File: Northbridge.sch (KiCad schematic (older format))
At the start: 25 parts, among them J3 JTAG

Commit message: Squiggles! Silk!
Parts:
- renumbered C106 to C301, C98 to C302, C99 to C303, C107 to C304, C100 to C305, C101 to C306, C115 to C307, C108 to C308, C102 to C309, C103 to C310, C109 to C311, C104 to C312, C105 to C313, C182 to C314, C184 to C315, C185 to C316, J3 to J301, R110 to R301, R111 to R302, R107 to R303, R39 to R304, R40 to R305, R118 to R306
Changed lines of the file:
@@
 AR Path="/5765B2E6/5799D8BC" Ref="C?"  Part="1"
 AR Path="/5763AB3B/5799D8BC" Ref="C?"  Part="1"
-AR Path="/5763A638/5799D8BC" Ref="C98"  Part="1"
-F 0 "C98" H 4513 13946 50  0000 L CNN
+AR Path="/5763A638/5799D8BC" Ref="C302"  Part="1"
+F 0 "C302" H 4513 13946 50  0000 L CNN
 F 1 "1u" H 4513 13855 50  0000 L CNN
 F 2 "IPC7351-Nominal:CAPC1005X55" H 4400 13900 50  0001 C CNN
@@
 AR Path="/5765B2E6/5799D8C4" Ref="C?"  Part="1"
 AR Path="/5763AB3B/5799D8C4" Ref="C?"  Part="1"
-AR Path="/5763A638/5799D8C4" Ref="C100"  Part="1"
-F 0 "C100" H 4913 13946 50  0000 L CNN
+AR Path="/5763A638/5799D8C4" Ref="C305"  Part="1"
+F 0 "C305" H 4913 13946 50  0000 L CNN
 F 1 "1u" H 4913 13855 50  0000 L CNN
 F 2 "IPC7351-Nominal:CAPC1005X55" H 4800 13900 50  0001 C CNN
@@
 AR Path="/5765B2E6/5799D8CC" Ref="C?"  Part="1"
 AR Path="/5763AB3B/5799D8CC" Ref="C?"  Part="1"
-AR Path="/5763A638/5799D8CC" Ref="C102"  Part="1"
-F 0 "C102" H 5313 13946 50  0000 L CNN
+AR Path="/5763A638/5799D8CC" Ref="C309"  Part="1"
+F 0 "C309" H 5313 13946 50  0000 L CNN
 F 1 "1u" H 5313 13855 50  0000 L CNN
 F 2 "IPC7351-Nominal:CAPC1005X55" H 5200 13900 50  0001 C CNN
@@
 AR Path="/5765B2E6/5799D8D4" Ref="C?"  Part="1"
 AR Path="/5763AB3B/5799D8D4" Ref="C?"  Part="1"
-AR Path="/5763A638/5799D8D4" Ref="C104"  Part="1"
-F 0 "C104" H 5713 13946 50  0000 L CNN
+AR Path="/5763A638/5799D8D4" Ref="C312"  Part="1"
+F 0 "C312" H 5713 13946 50  0000 L CNN
 F 1 "1u" H 5713 13855 50  0000 L CNN
 F 2 "IPC7351-Nominal:CAPC1005X55" H 5600 13900 50  0001 C CNN
@@
 AR Path="/5765B2E6/5799D8DC" Ref="C?"  Part="1"
 AR Path="/5763AB3B/5799D8DC" Ref="C?"  Part="1"
-AR Path="/5763A638/5799D8DC" Ref="C99"  Part="1"
-F 0 "C99" H 4513 14446 50  0000 L CNN
+AR Path="/5763A638/5799D8DC" Ref="C303"  Part="1"
+F 0 "C303" H 4513 14446 50  0000 L CNN
 F 1 "1u" H 4513 14355 50  0000 L CNN
 F 2 "IPC7351-Nominal:CAPC1005X55" H 4400 14400 50  0001 C CNN
@@
 AR Path="/5765B2E6/5799D8E4" Ref="C?"  Part="1"
 AR Path="/5763AB3B/5799D8E4" Ref="C?"  Part="1"
-AR Path="/5763A638/5799D8E4" Ref="C101"  Part="1"
-F 0 "C101" H 4913 14446 50  0000 L CNN
+AR Path="/5763A638/5799D8E4" Ref="C306"  Part="1"
+F 0 "C306" H 4913 14446 50  0000 L CNN
 F 1 "1u" H 4913 14355 50  0000 L CNN
 F 2 "IPC7351-Nominal:CAPC1005X55" H 4800 14400 50  0001 C CNN
@@
 AR Path="/5765B2E6/5799D8EC" Ref="C?"  Part="1"
 AR Path="/5763AB3B/5799D8EC" Ref="C?"  Part="1"
-AR Path="/5763A638/5799D8EC" Ref="C103"  Part="1"
-F 0 "C103" H 5313 14446 50  0000 L CNN
+AR Path="/5763A638/5799D8EC" Ref="C310"  Part="1"
+F 0 "C310" H 5313 14446 50  0000 L CNN
 F 1 "1u" H 5313 14355 50  0000 L CNN
 F 2 "IPC7351-Nominal:CAPC1005X55" H 5200 14400 50  0001 C CNN
@@
 AR Path="/5765B2E6/5799D8F4" Ref="C?"  Part="1"
 AR Path="/5763AB3B/5799D8F4" Ref="C?"  Part="1"
-AR Path="/5763A638/5799D8F4" Ref="C105"  Part="1"
-F 0 "C105" H 5713 14446 50  0000 L CNN
+AR Path="/5763A638/5799D8F4" Ref="C313"  Part="1"
+F 0 "C313" H 5713 14446 50  0000 L CNN
 F 1 "1u" H 5713 14355 50  0000 L CNN
 F 2 "IPC7351-Nominal:CAPC1005X55" H 5600 14400 50  0001 C CNN
@@
 P 5900 14700
 AR Path="/5763AB3B/5799D8FC" Ref="#PWR?"  Part="1"
-AR Path="/5763A638/5799D8FC" Ref="#PWR273"  Part="1"
-F 0 "#PWR273" H 5900 14700 30  0001 C CNN
+AR Path="/5763A638/5799D8FC" Ref="#PWR302"  Part="1"
+F 0 "#PWR302" H 5900 14700 30  0001 C CNN
 F 1 "GND" H 5900 14630 30  0001 C CNN
 F 2 "" H 5900 14700 60  0000 C CNN
@@
 AR Path="/5765B2E6/5799E7E9" Ref="C?"  Part="1"
 AR Path="/5763AB3B/5799E7E9" Ref="C?"  Part="1"
-AR Path="/5763A638/5799E7E9" Ref="C106"  Part="1"
-F 0 "C106" H 4513 12596 50  0000 L CNN
+AR Path="/5763A638/5799E7E9" Ref="C301"  Part="1"
+F 0 "C301" H 4513 12596 50  0000 L CNN
 F 1 "1u" H 4513 12505 50  0000 L CNN
 F 2 "IPC7351-Nominal:CAPC1005X55" H 4400 12550 50  0001 C CNN
@@
 AR Path="/5765B2E6/5799E7F0" Ref="C?"  Part="1"
 AR Path="/5763AB3B/5799E7F0" Ref="C?"  Part="1"
-AR Path="/5763A638/5799E7F0" Ref="C107"  Part="1"
-F 0 "C107" H 4913 12596 50  0000 L CNN
+AR Path="/5763A638/5799E7F0" Ref="C304"  Part="1"
+F 0 "C304" H 4913 12596 50  0000 L CNN
 F 1 "1u" H 4913 12505 50  0000 L CNN
 F 2 "IPC7351-Nominal:CAPC1005X55" H 4800 12550 50  0001 C CNN
@@
 AR Path="/5765B2E6/5799E7F7" Ref="C?"  Part="1"
 AR Path="/5763AB3B/5799E7F7" Ref="C?"  Part="1"
-AR Path="/5763A638/5799E7F7" Ref="C108"  Part="1"
-F 0 "C108" H 5313 12596 50  0000 L CNN
+AR Path="/5763A638/5799E7F7" Ref="C308"  Part="1"
+F 0 "C308" H 5313 12596 50  0000 L CNN
 F 1 "1u" H 5313 12505 50  0000 L CNN
 F 2 "IPC7351-Nominal:CAPC1005X55" H 5200 12550 50  0001 C CNN
@@
 AR Path="/5765B2E6/5799E7FE" Ref="C?"  Part="1"
 AR Path="/5763AB3B/5799E7FE" Ref="C?"  Part="1"
-AR Path="/5763A638/5799E7FE" Ref="C109"  Part="1"
-F 0 "C109" H 5713 12596 50  0000 L CNN
+AR Path="/5763A638/5799E7FE" Ref="C311"  Part="1"
+F 0 "C311" H 5713 12596 50  0000 L CNN
 F 1 "1u" H 5713 12505 50  0000 L CNN
 F 2 "IPC7351-Nominal:CAPC1005X55" H 5600 12550 50  0001 C CNN
@@
 P3V3_BRIDGE
 $Comp
-L GND #PWR272
+L GND #PWR301
 U 1 1 5799E8A3
 P 5600 12850
-F 0 "#PWR272" H 5600 12850 30  0001 C CNN
+F 0 "#PWR301" H 5600 12850 30  0001 C CNN
 F 1 "GND" H 5600 12780 30  0001 C CNN
 F 2 "" H 5600 12850 60  0000 C CNN
@@
 AR Path="/5765B2E6/579C48FF" Ref="C?"  Part="1"
 AR Path="/5763AB3B/579C48FF" Ref="C?"  Part="1"
-AR Path="/5763A638/579C48FF" Ref="C115"  Part="1"
-F 0 "C115" V 4750 13200 50  0000 C CNN
+AR Path="/5763A638/579C48FF" Ref="C307"  Part="1"
+F 0 "C307" V 4750 13200 50  0000 C CNN
 F 1 "1u" V 4841 13200 50  0000 C CNN
 F 2 "IPC7351-Nominal:CAPC1005X55" H 5000 13200 50  0001 C CNN
@@
 AR Path="/5765A5BA/57A59E23" Ref="R?"  Part="1"
 AR Path="/5765B2E6/57A59E23" Ref="R?"  Part="1"
-AR Path="/5763A638/57A59E23" Ref="R107"  Part="1"
-F 0 "R107" H 3713 2796 50  0000 L CNN
+AR Path="/5763A638/57A59E23" Ref="R303"  Part="1"
+F 0 "R303" H 3713 2796 50  0000 L CNN
 F 1 "330" H 3713 2705 50  0000 L CNN
 F 2 "IPC7351-Nominal:RESC1005X40" H 3650 2750 50  0001 C CNN
@@
 P3V3_BRIDGE
 $Comp
-L R-0402 R110
+L R-0402 R301
 U 1 1 57A5BAAA
 P 3550 3100
-F 0 "R110" V 3658 3100 50  0000 C CNN
+F 0 "R301" V 3658 3100 50  0000 C CNN
 F 1 "0R" V 3749 3100 50  0000 C CNN
 F 2 "IPC7351-Nominal:RESC1005X40" H 3550 3100 50  0001 C CNN
@@
 $EndComp
 $Comp
-L R-0402 R111
+L R-0402 R302
 U 1 1 57A5BEA9
 P 3550 4200
-F 0 "R111" V 3350 4200 50  0000 C CNN
+F 0 "R302" V 3350 4200 50  0000 C CNN
 F 1 "0R" V 3441 4200 50  0000 C CNN
 F 2 "IPC7351-Nominal:RESC1005X40" H 3550 4200 50  0001 C CNN
@@
 P 7500 14100
 AR Path="/5763AB3B/57A7C576" Ref="J?"  Part="1"
-AR Path="/5763A638/57A7C576" Ref="J3"  Part="1"
-F 0 "J3" H 7500 14340 50  0000 C CNN
+AR Path="/5763A638/57A7C576" Ref="J301"  Part="1"
+F 0 "J301" H 7500 14340 50  0000 C CNN
 F 1 "JTAG" H 7500 14249 50  0000 C CNN
 F 2 "conn-fci:98424-G52-14ALF" H 7475 14100 50  0001 C CNN
@@
 P 7200 14800
 AR Path="/5763AB3B/57A7C581" Ref="#PWR?"  Part="1"
-AR Path="/5763A638/57A7C581" Ref="#PWR274"  Part="1"
-F 0 "#PWR274" H 7200 14800 30  0001 C CNN
+AR Path="/5763A638/57A7C581" Ref="#PWR303"  Part="1"
+F 0 "#PWR303" H 7200 14800 30  0001 C CNN
 F 1 "GND" H 7200 14730 30  0001 C CNN
 F 2 "" H 7200 14800 60  0000 C CNN
@@
 P 7900 13900
 AR Path="/5763AB3B/57A7C596" Ref="R?"  Part="1"
-AR Path="/5763A638/57A7C596" Ref="R39"  Part="1"
-F 0 "R39" H 7963 13946 50  0000 L CNN
+AR Path="/5763A638/57A7C596" Ref="R304"  Part="1"
+F 0 "R304" H 7963 13946 50  0000 L CNN
 F 1 "5k1" H 7963 13855 50  0000 L CNN
 F 2 "IPC7351-Nominal:RESC1005X40" H 7900 13900 50  0001 C CNN
@@
 P 8200 13900
 AR Path="/5763AB3B/57A7C59E" Ref="R?"  Part="1"
-AR Path="/5763A638/57A7C59E" Ref="R40"  Part="1"
-F 0 "R40" H 8263 13946 50  0000 L CNN
+AR Path="/5763A638/57A7C59E" Ref="R305"  Part="1"
+F 0 "R305" H 8263 13946 50  0000 L CNN
 F 1 "5k1" H 8263 13855 50  0000 L CNN
 F 2 "IPC7351-Nominal:RESC1005X40" H 8200 13900 50  0001 C CNN
@@
 P 8900 14850
 AR Path="/5763AB3B/57A6F986" Ref="R?"  Part="1"
-AR Path="/5763A638/57A6F986" Ref="R118"  Part="1"
-F 0 "R118" H 8963 14896 50  0000 L CNN
+AR Path="/5763A638/57A6F986" Ref="R306"  Part="1"
+F 0 "R306" H 8963 14896 50  0000 L CNN
 F 1 "100k" H 8963 14805 50  0000 L CNN
 F 2 "IPC7351-Nominal:RESC1005X40" H 8900 14850 50  0001 C CNN
@@
 $EndComp
 $Comp
-L GND #PWR275
+L GND #PWR304
 U 1 1 57A6FC44
 P 8900 15000
-F 0 "#PWR275" H 8900 15000 30  0001 C CNN
+F 0 "#PWR304" H 8900 15000 30  0001 C CNN
 F 1 "GND" H 8900 14930 30  0001 C CNN
 F 2 "" H 8900 15000 60  0000 C CNN
@@
 AR Path="/5765B2E6/57AEA5DC" Ref="C?"  Part="1"
 AR Path="/5763AB3B/57AEA5DC" Ref="C?"  Part="1"
-AR Path="/5763A638/57AEA5DC" Ref="C182"  Part="1"
-F 0 "C182" H 11313 10846 50  0000 L CNN
+AR Path="/5763A638/57AEA5DC" Ref="C314"  Part="1"
+F 0 "C314" H 11313 10846 50  0000 L CNN
 F 1 "1u" H 11313 10755 50  0000 L CNN
 F 2 "IPC7351-Nominal:CAPC1005X55" H 11200 10800 50  0001 C CNN
@@
 PV75_SDRAM_VREF
 $Comp
-L GND #PWR276
+L GND #PWR305
 U 1 1 57AEAB10
 P 11200 11100
-F 0 "#PWR276" H 11200 11100 30  0001 C CNN
+F 0 "#PWR305" H 11200 11100 30  0001 C CNN
 F 1 "GND" H 11200 11030 30  0001 C CNN
 F 2 "" H 11200 11100 60  0000 C CNN
@@
 AR Path="/5765B2E6/57AEBA12" Ref="C?"  Part="1"
 AR Path="/5763AB3B/57AEBA12" Ref="C?"  Part="1"
-AR Path="/5763A638/57AEBA12" Ref="C184"  Part="1"
-F 0 "C184" H 11813 10846 50  0000 L CNN
+AR Path="/5763A638/57AEBA12" Ref="C315"  Part="1"
+F 0 "C315" H 11813 10846 50  0000 L CNN
 F 1 "1u" H 11813 10755 50  0000 L CNN
 F 2 "IPC7351-Nominal:CAPC1005X55" H 11700 10800 50  0001 C CNN
@@
 AR Path="/5765B2E6/57AECB4C" Ref="C?"  Part="1"
 AR Path="/5763AB3B/57AECB4C" Ref="C?"  Part="1"
-AR Path="/5763A638/57AECB4C" Ref="C185"  Part="1"
-F 0 "C185" H 12313 10846 50  0000 L CNN
+AR Path="/5763A638/57AECB4C" Ref="C316"  Part="1"
+F 0 "C316" H 12313 10846 50  0000 L CNN
 F 1 "1u" H 12313 10755 50  0000 L CNN
 F 2 "IPC7351-Nominal:CAPC1005X55" H 12200 10800 50  0001 C CNN

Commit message: Final BOM
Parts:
- R303: value 330 -> 750; BOM RES SMD 330 1% [0402] -> RES SMD 750 [0402]
- R304, R305: value 5k1 -> 4k3; BOM RES SMD 5k1 1% [0402] -> RES SMD 4k3 [0402]
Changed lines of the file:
@@
 AR Path="/5763A638/57A59E23" Ref="R303"  Part="1"
 F 0 "R303" H 3713 2796 50  0000 L CNN
-F 1 "330" H 3713 2705 50  0000 L CNN
+F 1 "750" H 3713 2705 50  0000 L CNN
 F 2 "IPC7351-Nominal:RESC1005X40" H 3650 2750 50  0001 C CNN
 F 3 "" H 3650 2800 60  0000 C CNN
-F 4 "RES SMD 330 1% [0402]" H 4400 3300 60  0001 C CNN "BOM"
+F 4 "RES SMD 750 [0402]" H 4400 3300 60  0001 C CNN "BOM"
 	1    3650 2750
 	1    0    0    -1
@@
 AR Path="/5763A638/57A7C596" Ref="R304"  Part="1"
 F 0 "R304" H 7963 13946 50  0000 L CNN
-F 1 "5k1" H 7963 13855 50  0000 L CNN
+F 1 "4k3" H 7963 13855 50  0000 L CNN
 F 2 "IPC7351-Nominal:RESC1005X40" H 7900 13900 50  0001 C CNN
 F 3 "" H 7900 13950 60  0000 C CNN
-F 4 "RES SMD 5k1 1% [0402]" H 8650 14450 60  0001 C CNN "BOM"
+F 4 "RES SMD 4k3 [0402]" H 8650 14450 60  0001 C CNN "BOM"
 	1    7900 13900
 	1    0    0    -1
@@
 AR Path="/5763A638/57A7C59E" Ref="R305"  Part="1"
 F 0 "R305" H 8263 13946 50  0000 L CNN
-F 1 "5k1" H 8263 13855 50  0000 L CNN
+F 1 "4k3" H 8263 13855 50  0000 L CNN
 F 2 "IPC7351-Nominal:RESC1005X40" H 8200 13900 50  0001 C CNN
 F 3 "" H 8200 13950 60  0000 C CNN
-F 4 "RES SMD 5k1 1% [0402]" H 8950 14450 60  0001 C CNN "BOM"
+F 4 "RES SMD 4k3 [0402]" H 8950 14450 60  0001 C CNN "BOM"
 	1    8200 13900
 	1    0    0    -1

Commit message: Remove current sense resistors, add I2C debug header
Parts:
- removed BRIDGE1: XC6SLX25-FGG484, manuf:XILINX-FGG484, symbol XC6SLX25-FGG484
- added BRIDGE1: XC6SLX45-FGG484, manuf:XILINX-FGG484, symbol XC6SLX45-FGG484
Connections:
- wire segments 497 -> 498
- no-connect marks 17 -> 16
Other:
- moved on the sheet: C301, C302, C303, C304, C305, C306, C307, C308, C309, C310, C311, C312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

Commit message: sdram weeeee
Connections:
- net labels added: BANK0, BANK1, BANK3
- net labels removed: CPU_D11, CPU_D15, CPU_D16, CPU_D19, CPU_D20, CPU_D31
- wire segments 498 -> 743
- no-connect marks 16 -> 6

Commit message: Reroute CPU bus
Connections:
- net labels added: CPU_CLK_IN, CPU_CLK_OUT, CPU_D11, CPU_D15, CPU_D16, CPU_D19, CPU_D20, CPU_D31
- net labels removed: CPU_CLK
- wire segments 743 -> 667

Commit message: Route some PCIs
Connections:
- net labels added: BANK2
- wire segments 667 -> 758
- no-connect marks 6 -> 5

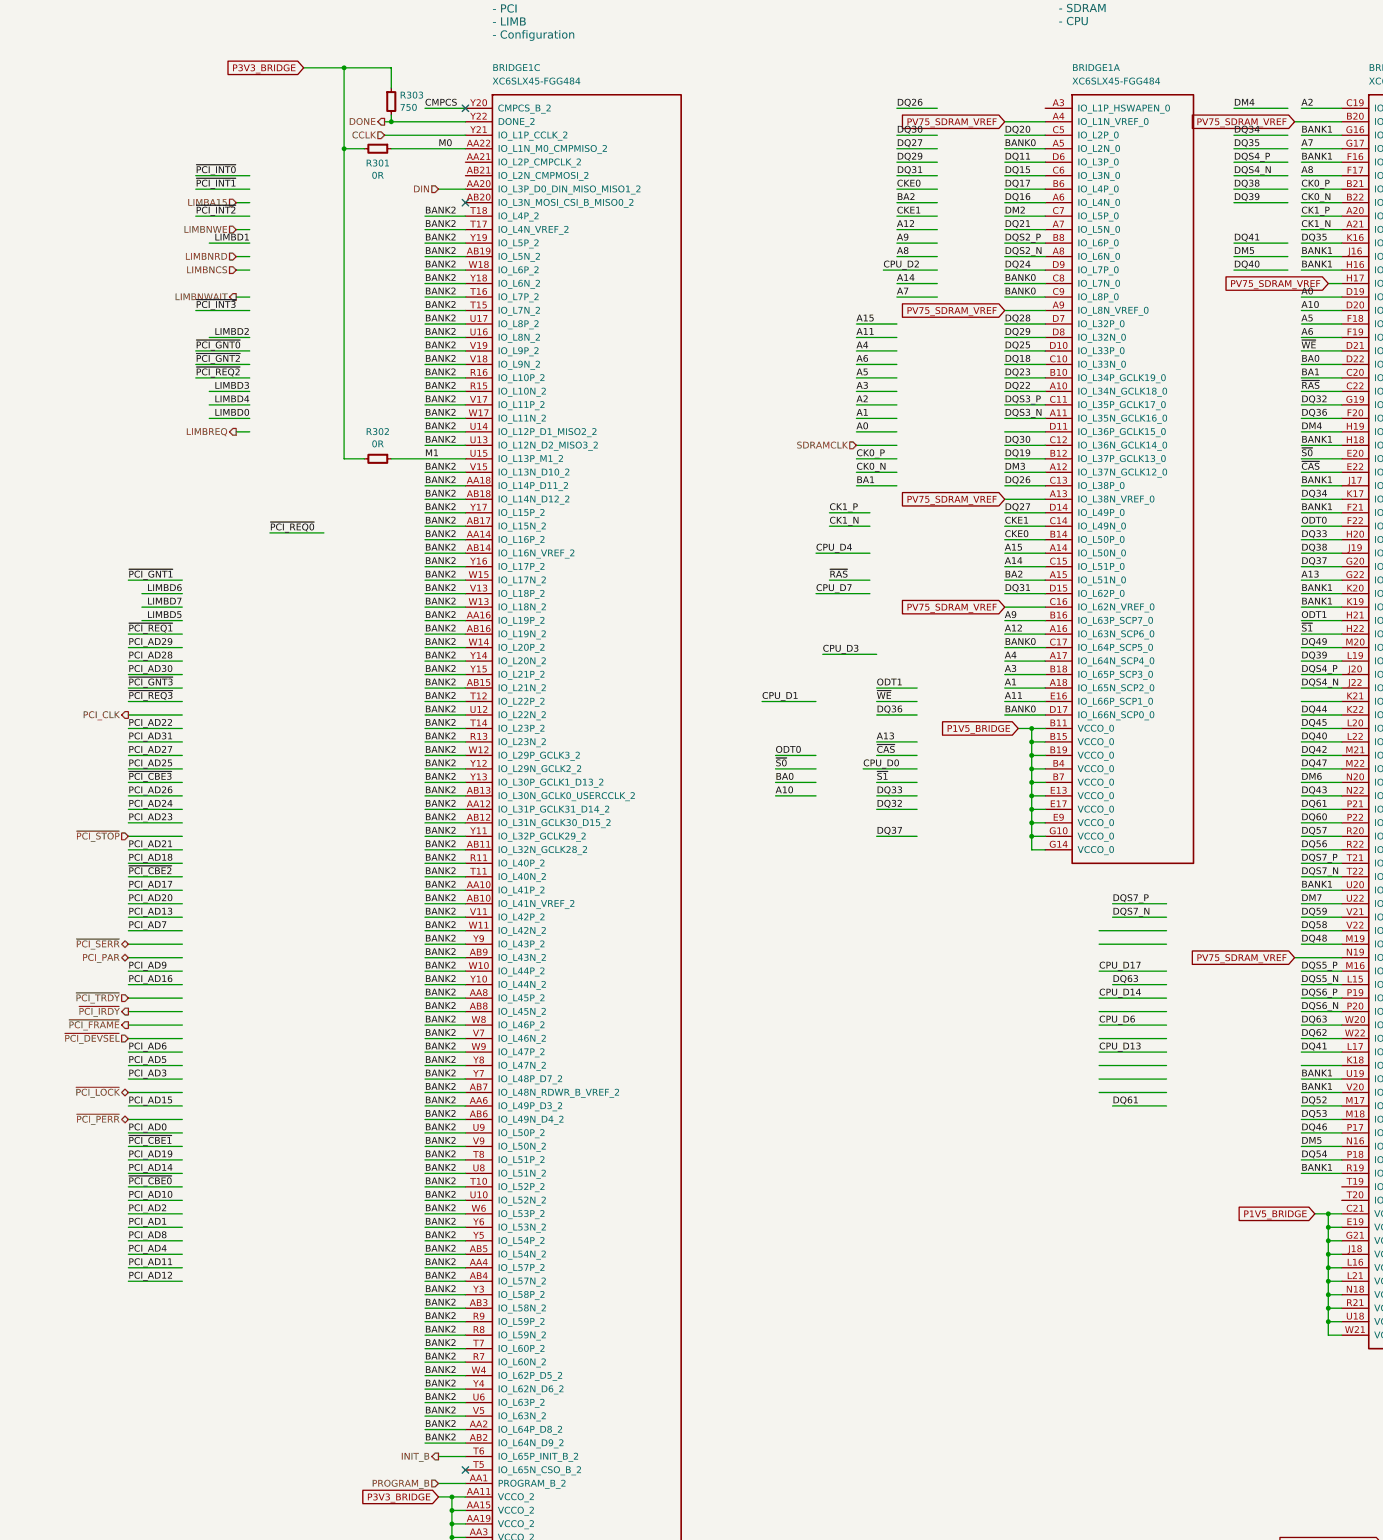
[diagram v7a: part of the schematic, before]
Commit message: Route PCI bus. again.
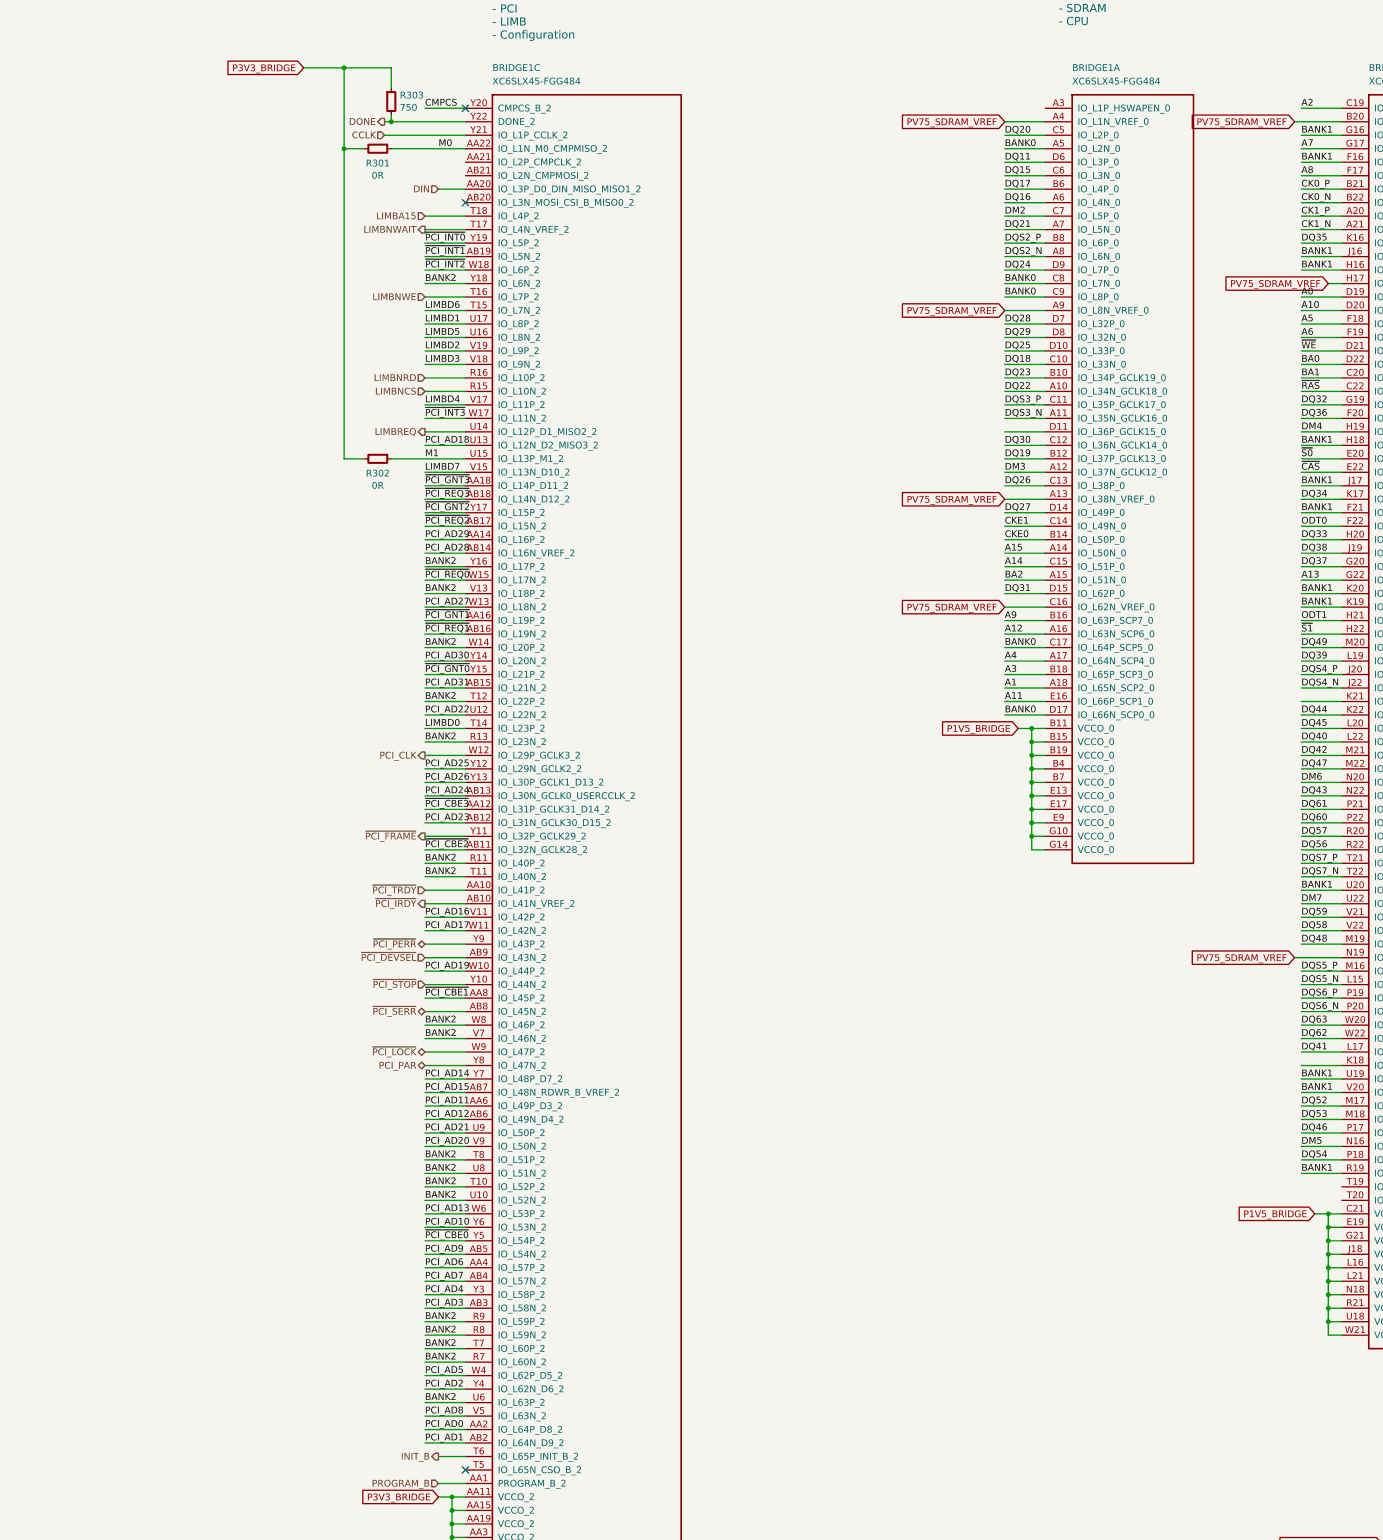
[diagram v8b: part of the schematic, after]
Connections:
- net labels removed: SDRAMCLK
- wire segments 758 -> 613
